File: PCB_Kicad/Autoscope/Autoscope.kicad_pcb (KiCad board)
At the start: 2 copper layers, 85 x 56 mm, 14 parts, among them J1 Conn_01x02, J10 Conn_01x04, J11 Conn_01x04, J12 Conn_01x04, J2 Conn_01x02, J3 Conn_01x02, J4 Conn_01x02, J5 Conn_01x02, J6 Conn_01x02, J7 Conn_01x04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

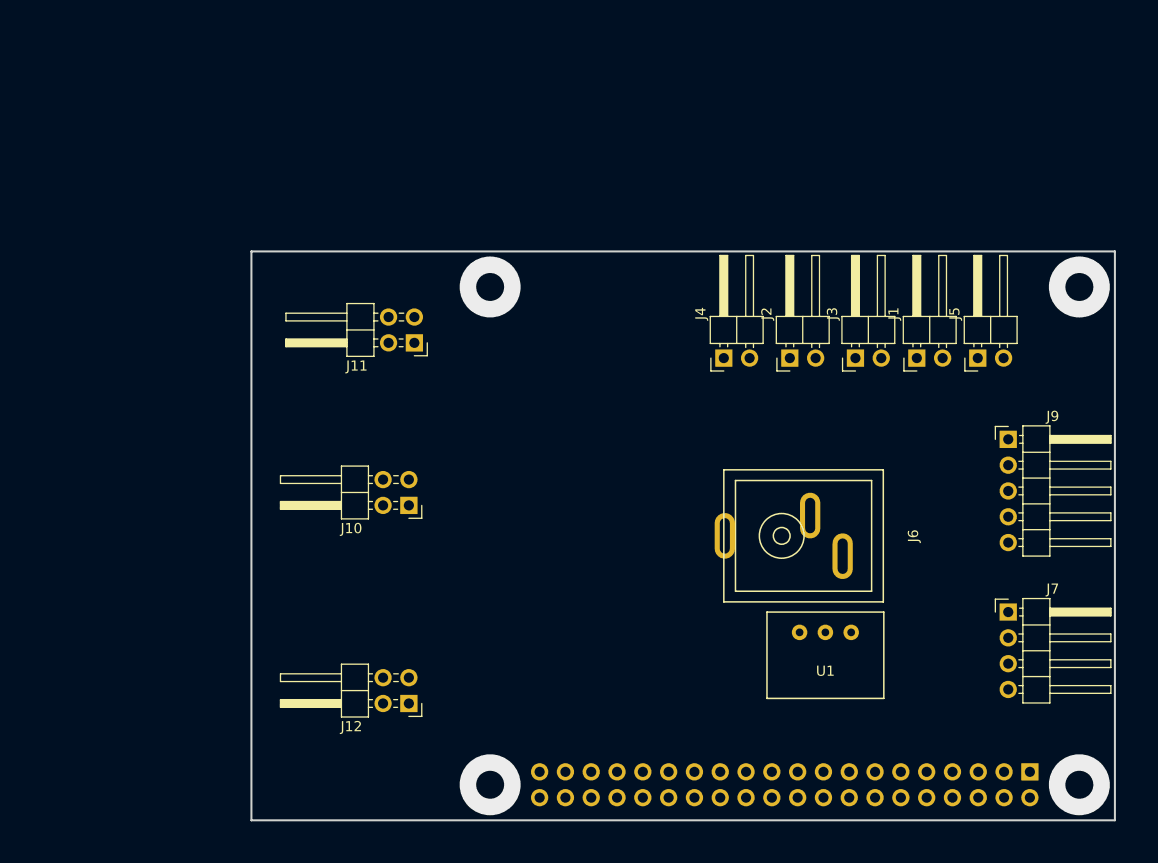
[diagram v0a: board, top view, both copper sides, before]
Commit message: schematic ok & pcb in progress
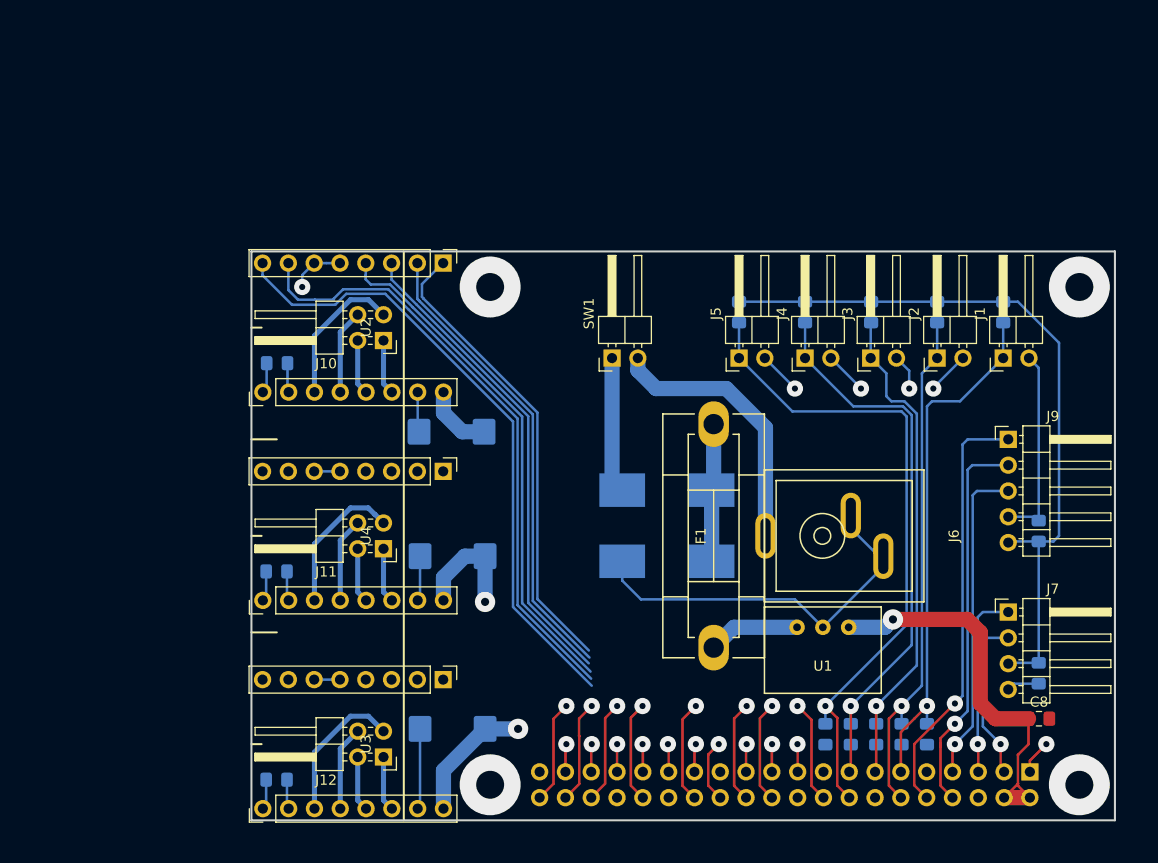
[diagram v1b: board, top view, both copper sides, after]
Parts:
- added C1: 100nF, Capacitor_SMD:C_0805_2012Metric_Pad1.15x1.40mm_HandSolder, B.Cu at (146.5, 97.5)
- added C10: 100µF, Capacitor_Tantalum_SMD:CP_EIA-7343-43_Kemet-X_Pad2.25x2.55mm_HandSolder, B.Cu at (99.8, 80.0)
- added C11: 100µF, Capacitor_Tantalum_SMD:CP_EIA-7343-43_Kemet-X_Pad2.25x2.55mm_HandSolder, B.Cu at (99.8, 97.0)
- added C12: 100nF, Capacitor_SMD:C_0805_2012Metric_Pad1.15x1.40mm_HandSolder, B.Cu at (82.5, 61.0)
- added C13: 100nF, Capacitor_SMD:C_0805_2012Metric_Pad1.15x1.40mm_HandSolder, B.Cu at (82.5, 81.5)
- added C14: 100nF, Capacitor_SMD:C_0805_2012Metric_Pad1.15x1.40mm_HandSolder, B.Cu at (82.5, 102.0)
- added C2: 100nF, Capacitor_SMD:C_0805_2012Metric_Pad1.15x1.40mm_HandSolder, B.Cu at (144.0, 97.5)
- added C3: 100nF, Capacitor_SMD:C_0805_2012Metric_Pad1.15x1.40mm_HandSolder, B.Cu at (141.5, 97.5)
- added C4: 100nF, Capacitor_SMD:C_0805_2012Metric_Pad1.15x1.40mm_HandSolder, B.Cu at (139.0, 97.5)
- added C5: 100nF, Capacitor_SMD:C_0805_2012Metric_Pad1.15x1.40mm_HandSolder, B.Cu at (136.5, 97.5)
- added C6: 100nF, Capacitor_SMD:C_0805_2012Metric_Pad1.15x1.40mm_HandSolder, B.Cu at (157.5, 91.5)
- added C7: 100nF, Capacitor_SMD:C_0805_2012Metric_Pad1.15x1.40mm_HandSolder, B.Cu at (157.5, 77.5)
- added C8: 100nF, Capacitor_SMD:C_0805_2012Metric_Pad1.15x1.40mm_HandSolder, F.Cu at (157.5, 96.0)
- added C9: 100µF, Capacitor_Tantalum_SMD:CP_EIA-7343-43_Kemet-X_Pad2.25x2.55mm_HandSolder, B.Cu at (99.7, 67.8)
- added D1: Schottky, Diode_SMD:D_SMC_Handsoldering, B.Cu at (120.9, 73.5)
- added D2: 14V, Diode_SMD:D_SMC_Handsoldering, B.Cu at (120.9, 80.5)
- added F1: 3A, Autoscope:Fuseholder5x20_horiz_SemiClosed_Casing10x25mm, F.Cu at (125.5, 78.0)
- added R1: 100kR, Resistor_SMD:R_0805_2012Metric_Pad1.15x1.40mm_HandSolder, B.Cu at (154.0, 56.0)
- added R2: 100kR, Resistor_SMD:R_0805_2012Metric_Pad1.15x1.40mm_HandSolder, B.Cu at (147.5, 56.0)
- added R3: 100kR, Resistor_SMD:R_0805_2012Metric_Pad1.15x1.40mm_HandSolder, B.Cu at (141.0, 56.0)
- added R4: 100kR, Resistor_SMD:R_0805_2012Metric_Pad1.15x1.40mm_HandSolder, B.Cu at (134.5, 56.0)
- added R5: 100kR, Resistor_SMD:R_0805_2012Metric_Pad1.15x1.40mm_HandSolder, B.Cu at (128.0, 56.0)
- added SW1: SW_SPST, Connector_PinHeader_2.54mm:PinHeader_1x02_P2.54mm_Horizontal, F.Cu at (115.5, 60.5)
- added U2: A4988, Autoscope:A4988, F.Cu at (90.0, 57.5)
- added U3: A4988, Autoscope:A4988, F.Cu at (90.0, 98.5)
- added U4: A4988, Autoscope:A4988, F.Cu at (90.0, 78.0)
- J10, J11, J12: value Conn_01x04 -> Conn_02x02_Odd_Even
- moved J5 23.5 mm to (128.0, 60.5)
- moved J11 20.5 mm to (93.0, 79.3)
- moved J10 16.4 mm to (93.0, 58.8)
- moved J2 14.5 mm to (147.5, 60.5)
- moved G*** 12.6 mm to (116.5, 75.2), turned to 90 degrees
- moved J1 8.50 mm to (154.0, 60.5)
- moved J4 8.00 mm to (134.5, 60.5)
- moved J12 5.83 mm to (93.0, 99.8)
- moved J6 4.00 mm to (139.0, 78.0)
- moved J3 1.50 mm to (141.0, 60.5)
- moved U1 0.56 mm to (136.2, 87.0)
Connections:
- J10 pad 1: Net-(J10-Pad1) -> /Motor1_2B
- J10 pad 2: Net-(J10-Pad2) -> /Motor1_2A
- J10 pad 3: Net-(J10-Pad3) -> /Motor1_1B
- J10 pad 4: Net-(J10-Pad4) -> /Motor1_1A
- J11 pad 1: Net-(J11-Pad1) -> /Motor2_2B
- J11 pad 2: Net-(J11-Pad2) -> /Motor2_2A
- J11 pad 3: Net-(J11-Pad3) -> /Motor2_1B
- J11 pad 4: Net-(J11-Pad4) -> /Motor2_1A
- J12 pad 1: Net-(J12-Pad1) -> /Motor3_2B
- J12 pad 2: Net-(J12-Pad2) -> /Motor3_2A
- J12 pad 3: Net-(J12-Pad3) -> /Motor3_1B
- J12 pad 4: Net-(J12-Pad4) -> /Motor3_1A
- J8 pad 10: /GPS_Tx -> /GPS_EN
- J8 pad 11: /Position_sensor_2 -> /Position_sensor_1
- J8 pad 12: /GPS_EN -> /Position_sensor_2
- J8 pad 16: /Posotion_sensor_5 -> /Position_sensor_5
- J8 pad 7: /Position_sensor_1 -> /GPS_Rx
- J8 pad 8: /GPS_Rx -> /GPS_Tx
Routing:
- net GND: track 0.00 -> 102.9 mm, vias 0 -> 8
- net +3V3: track 0.00 -> 95.1 mm, vias 0 -> 2
- net /Motor1_DIR: track 0.00 -> 72.0 mm, vias 0 -> 1
- net /Position_sensor_5: track 0.00 -> 65.9 mm, vias 0 -> 1
- net /Motor1_STEP: track 0.00 -> 62.7 mm, vias 0 -> 1
- net /Motor1_MS2: track 0.00 -> 57.4 mm, vias 0 -> 1
- net /Motor1_EN: track 0.00 -> 55.8 mm, vias 0 -> 1
- net /Position_sensor_4: track 0.00 -> 55.5 mm, vias 0 -> 1
- net /Motor1_MS3: track 0.00 -> 53.2 mm, vias 0 -> 1
- net /Position_sensor_1: track 0.00 -> 51.8 mm, vias 0 -> 1
- net /Position_sensor_2: track 0.00 -> 51.0 mm, vias 0 -> 1
- net /Position_sensor_3: track 0.00 -> 50.1 mm, vias 0 -> 1
- net /Motor1_MS1: track 0.00 -> 48.7 mm, vias 0 -> 1
- net /GPS_EN: track 0.00 -> 41.9 mm, vias 0 -> 1
- net +12V: track 0.00 -> 40.4 mm, vias 0 -> 2
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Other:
- net class Default: via_dia 0.8 -> 1.6; via_drill 0.4 -> 0.6
- net class Power 1A added: clearance 0.2, trace_width 0.5, via_dia 1.6, via_drill 0.6
- net class Power 3A added: clearance 0.2, trace_width 1.5, via_dia 2, via_drill 0.8

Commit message: nearly finished pcb
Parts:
- moved G*** 5.49 mm to (111.8, 78.0)
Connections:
- J8 pad 18: /Motor1_DIR -> /Motor1_EN
- J8 pad 19: /Motor1_STEP -> /Motor1_MS3
- J8 pad 21: /Motor1_MS3 -> /Motor1_STEP
- J8 pad 22: /Motor1_MS2 -> /Motor1_MS1
- J8 pad 23: /Motor1_MS1 -> /Motor1_DIR
- J8 pad 24: /Motor1_EN -> /Motor1_MS2
- J8 pad 26: /Motor2_DIR -> /Motor2_EN
- J8 pad 27: /Motor2_STEP -> /Motor2_MS1
- J8 pad 28: /Motor2_MS3 -> /Motor2_MS2
- J8 pad 29: /Motor2_MS2 -> /Motor2_MS3
- J8 pad 31: /Motor2_MS1 -> /Motor2_DIR
- J8 pad 32: /Motor2_EN -> /Motor2_STEP
- J8 pad 33: /Motor3_DIR -> /Motor3_MS2
- J8 pad 35: /Motor3_MS2 -> /Motor3_MS1
- J8 pad 36: /Motor3_STEP -> /Motor3_MS3
- J8 pad 37: /Motor3_MS3 -> /Motor3_EN
- J8 pad 38: /Motor3_MS1 -> /Motor3_STEP
- J8 pad 40: /Motor3_EN -> /Motor3_DIR
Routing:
- net GND: track 102.9 -> 534.7 mm, vias 8 -> 15
- net +3V3: track 95.1 -> 230.5 mm, vias 2 -> 6
- net +12V: track 40.4 -> 100.2 mm, vias 2 -> 3
- net /Motor2_STEP: track 2.79 -> 61.6 mm
- net /Motor2_DIR: track 6.18 -> 60.2 mm
- net /Motor2_MS2: track 2.76 -> 54.1 mm
- net /Motor2_MS1: track 2.74 -> 50.4 mm
- net /Motor2_MS3: track 10.1 -> 52.6 mm
- net /Motor2_EN: track 9.98 -> 52.5 mm
- net +5V: track 39.3 -> 81.3 mm
- net /Motor3_DIR: track 2.73 -> 43.6 mm
- net /Motor3_MS3: track 2.77 -> 38.9 mm
- net /Motor3_STEP: track 10.1 -> 44.1 mm
- net /Motor1_MS1: track 48.7 -> 76.9 mm
- net /Motor3_MS2: track 2.75 -> 28.9 mm
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- added copper zone on B.Cu, net GND
- added copper zone on F.Cu, net GND
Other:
- board text added: "AUTOSCOPE v1.0"
- board text added: "AZIM"
- board text added: "ELEV"
- board text added: "GPS"
- board text added: "IMU"
- board text added: "ON/OFF"
- board text added: "SA1"
- board text added: "SE1"
- board text added: "SE2"
- board text added: "SZ1"
- board text added: "SZ2"
- board text added: "ZOOM"

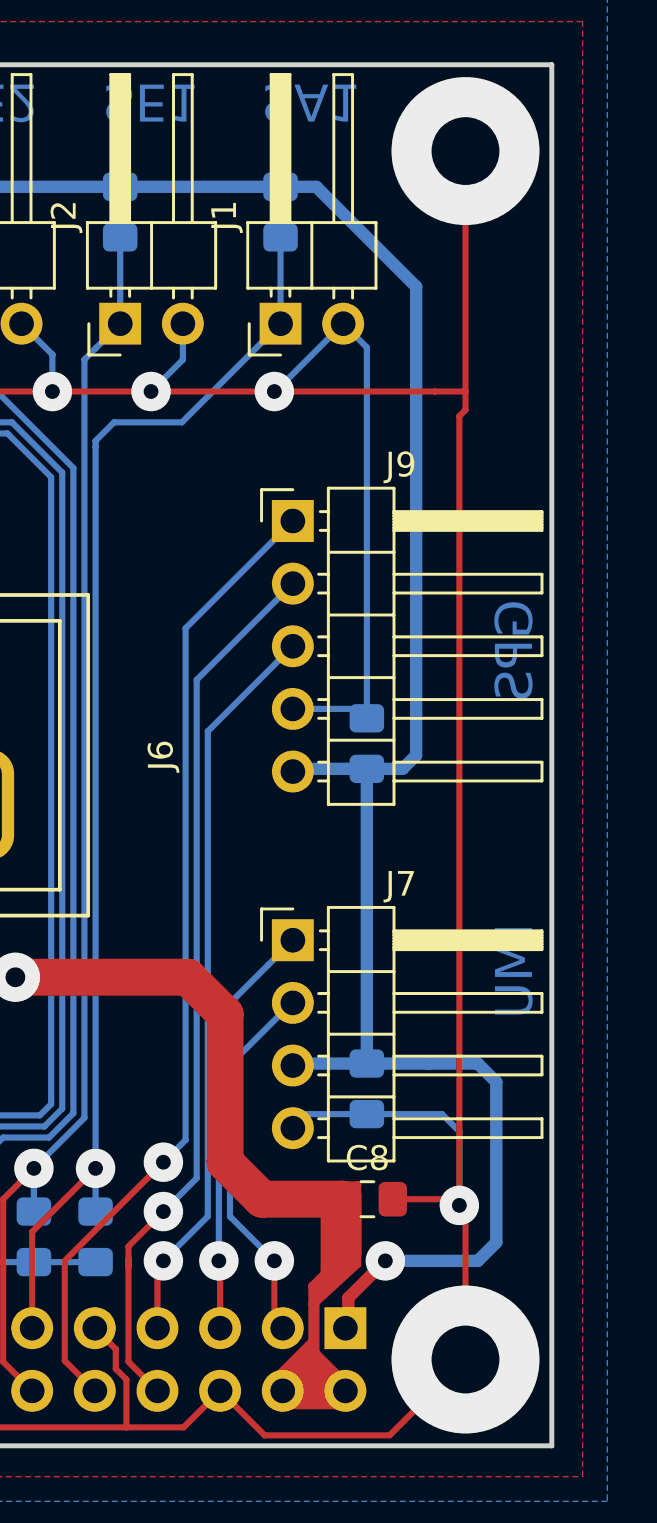
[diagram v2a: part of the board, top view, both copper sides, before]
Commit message: add BOM
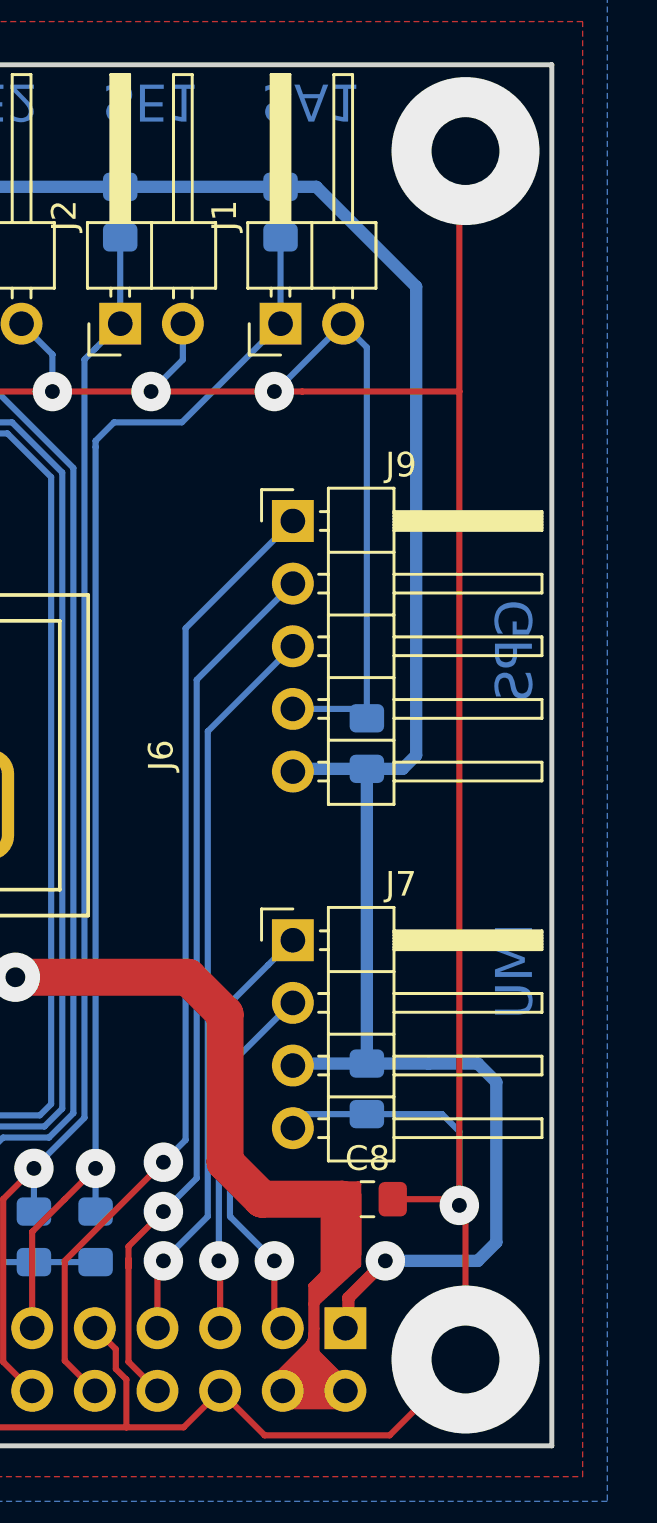
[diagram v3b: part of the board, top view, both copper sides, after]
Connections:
- J8 pad 17: +3V3 -> Net-(J8-Pad17)
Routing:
- net +5V: track 81.3 -> 84.4 mm
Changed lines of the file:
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@@
     (thickness 1.6)
     (drawings 22)
-    (tracks 661)
+    (tracks 662)
     (zones 0)
     (modules 40)
-    (nets 48)
+    (nets 49)
   )
   (page A4)
@@
   (net 46 "Net-(D1-Pad2)")
   (net 47 "Net-(D1-Pad1)")
+  (net 48 "Net-(J8-Pad17)")
   (net_class Default "This is the default net class."
     (clearance 0.2)
@@
     (add_net /Position_sensor_5)
     (add_net GND)
+    (add_net "Net-(J8-Pad17)")
   )
   (net_class "Power 1A" ""
@@
       (net 32 /Position_sensor_5))
     (pad 17 thru_hole oval (at 0 -20.32 90) (size 1.7 1.7) (drill 1) (layers *.Cu *.Mask)
-      (net 4 +3V3))
+      (net 48 "Net-(J8-Pad17)"))
     (pad 18 thru_hole oval (at -2.54 -20.32 90) (size 1.7 1.7) (drill 1) (layers *.Cu *.Mask)
       (net 19 /Motor1_EN))
@@
   (segment (start 161 96) (end 161.25 96.25) (width 0.25) (layer F.Cu) (net 2))
   (segment (start 158.55 96) (end 161 96) (width 0.25) (layer F.Cu) (net 2))
-  (segment (start 153.75 63.25) (end 160.25 63.25) (width 0.25) (layer F.Cu) (net 2))
-  (segment (start 161.25 64.25) (end 161.25 96.25) (width 0.25) (layer F.Cu) (net 2))
   (segment (start 161.5 102.5) (end 158.42501 105.57499) (width 0.25) (layer F.Cu) (net 2))
   (segment (start 153.35499 105.57499) (end 151.55 103.77) (width 0.25) (layer F.Cu) (net 2))
@@
   (segment (start 103.5 53.5) (end 115.75 53.5) (width 0.25) (layer F.Cu) (net 2))
   (segment (start 115.75 53.5) (end 125.5 63.25) (width 0.25) (layer F.Cu) (net 2))
-  (segment (start 161.25 64.25) (end 161.5 64) (width 0.25) (layer F.Cu) (net 2))
-  (segment (start 160.25 63.25) (end 161.5 63.25) (width 0.25) (layer F.Cu) (net 2))
-  (segment (start 161.5 64) (end 161.5 63.25) (width 0.25) (layer F.Cu) (net 2))
-  (segment (start 161.5 63.25) (end 161.5 53.5) (width 0.25) (layer F.Cu) (net 2))
   (segment (start 88.05 101.25) (end 96.6 101.25) (width 0.25) (layer F.Cu) (net 2))
   (segment (start 81.45 94.65) (end 88.05 101.25) (width 0.25) (layer F.Cu) (net 2))
@@
   (segment (start 81.45 94.65) (end 82.65 94.65) (width 0.25) (layer B.Cu) (net 2))
   (segment (start 82.65 94.65) (end 83 95) (width 0.25) (layer B.Cu) (net 2))
+  (segment (start 161.25 53.75) (end 161.5 53.5) (width 0.25) (layer F.Cu) (net 2))
+  (segment (start 154.88137 63.25) (end 161.25 63.25) (width 0.25) (layer F.Cu) (net 2))
+  (segment (start 153.75 63.25) (end 154.88137 63.25) (width 0.25) (layer F.Cu) (net 2))
+  (segment (start 161.25 96.25) (end 161.25 63.25) (width 0.25) (layer F.Cu) (net 2))
+  (segment (start 161.25 63.25) (end 161.25 53.75) (width 0.25) (layer F.Cu) (net 2))
   (segment (start 154.09 103.77) (end 156.63 103.77) (width 1.5) (layer F.Cu) (net 3))
   (segment (start 154.09 103.77) (end 155.454999 102.405001) (width 0.25) (layer F.Cu) (net 3))
@@
   (segment (start 157.15 98.26) (end 157.15 95.4) (width 0.25) (layer F.Cu) (net 3))
   (segment (start 157.15 95.4) (end 154.29 95.4) (width 0.25) (layer F.Cu) (net 3))
+  (segment (start 154.885001 102.364999) (end 155.454999 101.25) (width 0.25) (layer F.Cu) (net 3))
+  (segment (start 155 103) (end 155.319998 101.135001) (width 0.25) (layer F.Cu) (net 3))
   (segment (start 154.58 90.5) (end 154.5 90.58) (width 0.25) (layer B.Cu) (net 4))
   (segment (start 157.5 90.5) (end 154.58 90.5) (width 0.5) (layer B.Cu) (net 4))

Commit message: really nearly finished pcb & 3D models
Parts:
- U1: footprint Autoscope:R-78B-2.0 -> Converter_DCDC:Converter_DCDC_RECOM_R-78B-2.0_THT
- moved U1 2.50 mm to (133.8, 87.0)
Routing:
- net GND: track 534.5 -> 513.3 mm
- net +3V3: track 230.5 -> 237.6 mm
- net Net-(J6-Pad1): track 26.8 -> 26.0 mm
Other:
- net class Default: via_dia 1.6 -> 1.8

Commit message: finalize PCB files
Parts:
- J6: value Conn_01x02 -> 12VDC Supply
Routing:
- net GND: track 513.3 -> 515.5 mm

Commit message: ready to print PCB
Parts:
- added C15: 100µF, Capacitor_Tantalum_SMD:CP_EIA-7343-43_Kemet-X_Pad2.25x2.55mm_HandSolder, B.Cu at (115.8, 56.8)
- added J13: Conn_01x02, Connector_PinHeader_2.54mm:PinHeader_1x02_P2.54mm_Horizontal, F.Cu at (112.5, 60.5)
- SW1: value SW_SPST -> Conn_01x02
- moved SW1 3.46 mm to (119.0, 60.5)
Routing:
- net GND: track 515.5 -> 574.1 mm
- net +12V: track 100.2 -> 123.4 mm, vias 3 -> 4
- net Net-(J6-Pad1): track 26.0 -> 22.6 mm
- net +3V3: track 237.6 -> 239.1 mm
- net Net-(D1-Pad2): track 13.4 -> 14.0 mm
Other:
- board text added: "FAN"
- board text added: "ON"
- board text removed: "ON/OFF"

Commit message: add A5 fab files
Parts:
- moved C12 28.3 mm to (62.5, 41.0)
- moved C7 28.3 mm to (137.5, 57.5)
- moved J3 28.3 mm to (121.0, 40.5)
- moved C1 28.3 mm to (126.5, 77.5)
- moved C10 28.3 mm to (79.8, 60.0)
- moved C11 28.3 mm to (79.8, 77.0)
- moved C15 28.3 mm to (95.8, 36.8)
- moved C2 28.3 mm to (124.0, 77.5)
- moved C3 28.3 mm to (121.5, 77.5)
- moved C4 28.3 mm to (119.0, 77.5)
- moved C5 28.3 mm to (116.5, 77.5)
- moved C6 28.3 mm to (137.5, 71.5)
- moved C8 28.3 mm to (137.5, 76.0)
- moved C9 28.3 mm to (79.7, 47.8)
- moved D1 28.3 mm to (100.9, 53.5)
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
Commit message: Revert "add A5 fab files"
This reverts commit e4fdc3836b1555d306f2fe8898c2b94182f1870a.
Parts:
- moved C12 28.3 mm to (82.5, 61.0)
- moved C7 28.3 mm to (157.5, 77.5)
- moved J3 28.3 mm to (141.0, 60.5)
- moved C1 28.3 mm to (146.5, 97.5)
- moved C10 28.3 mm to (99.8, 80.0)
- moved C11 28.3 mm to (99.8, 97.0)
- moved C15 28.3 mm to (115.8, 56.8)
- moved C2 28.3 mm to (144.0, 97.5)
- moved C3 28.3 mm to (141.5, 97.5)
- moved C4 28.3 mm to (139.0, 97.5)
- moved C5 28.3 mm to (136.5, 97.5)
- moved C6 28.3 mm to (157.5, 91.5)
- moved C8 28.3 mm to (157.5, 96.0)
- moved C9 28.3 mm to (99.7, 67.8)
- moved D1 28.3 mm to (120.9, 73.5)
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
